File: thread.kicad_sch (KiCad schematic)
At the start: 1 part, among them U1 nRF52840

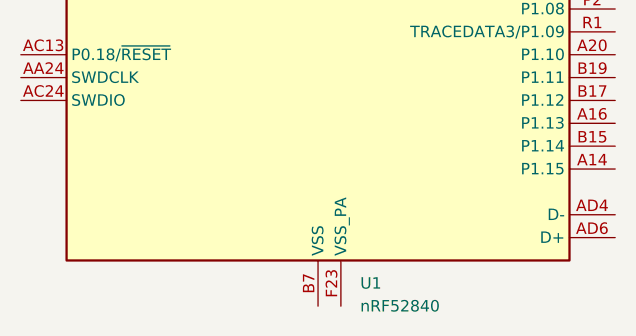
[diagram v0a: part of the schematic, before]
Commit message: Fixed schematic symbol errors
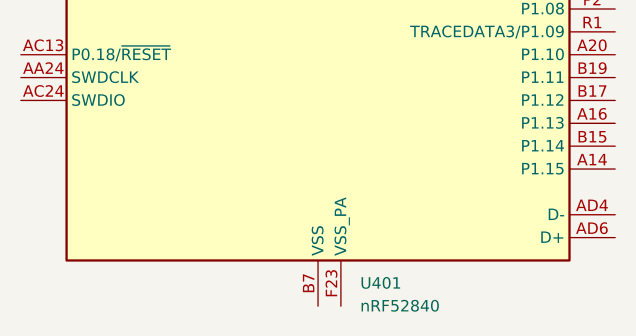
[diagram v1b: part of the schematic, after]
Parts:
- renumbered U1 to U401
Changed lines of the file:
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@@
 		(dnp no)
 		(fields_autoplaced yes)
-		(property "Reference" "U1"
+		(property "Reference" "U401"
 			(at 146.9233 212.09 0)
 			(effects
@@
 			(project ""
 				(path "/b43b7bca-e50d-42ec-8ff0-e0016dfefe0a/ab846a80-6f2e-4d25-9090-1f6af1d6fbdd"
-					(reference "U1")
+					(reference "U401")
 					(unit 1)
 				)

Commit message: Added some net labels and schematic routing
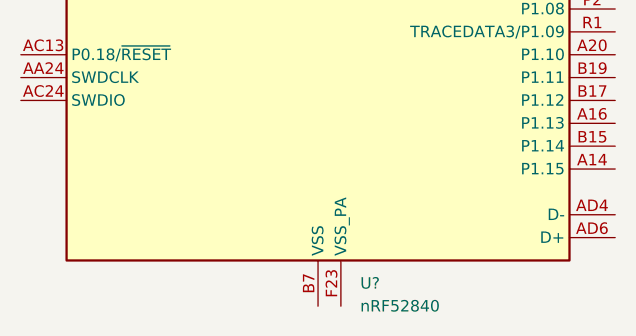
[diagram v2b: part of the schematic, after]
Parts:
- renumbered U401 to U?
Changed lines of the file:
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@@
 		(dnp no)
 		(fields_autoplaced yes)
-		(property "Reference" "U401"
+		(property "Reference" "U?"
 			(at 146.9233 212.09 0)
 			(effects
@@
 			(project ""
 				(path "/b43b7bca-e50d-42ec-8ff0-e0016dfefe0a/ab846a80-6f2e-4d25-9090-1f6af1d6fbdd"
-					(reference "U401")
+					(reference "U?")
 					(unit 1)
 				)

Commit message: Worked on schematic for DDR4 memory
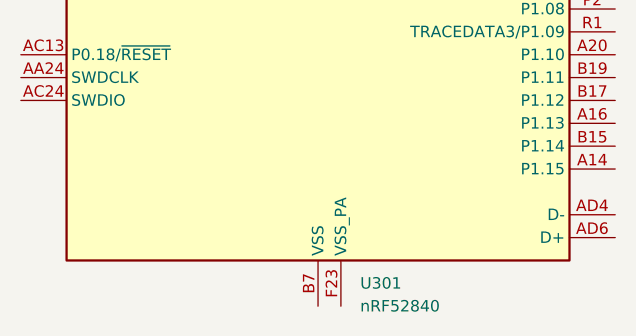
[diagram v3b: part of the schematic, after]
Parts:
- gave numbers to parts that had none: 1
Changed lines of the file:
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@@
 		(dnp no)
 		(fields_autoplaced yes)
-		(property "Reference" "U?"
+		(property "Reference" "U301"
 			(at 146.9233 212.09 0)
 			(effects
@@
 			(project ""
 				(path "/b43b7bca-e50d-42ec-8ff0-e0016dfefe0a/ab846a80-6f2e-4d25-9090-1f6af1d6fbdd"
-					(reference "U?")
+					(reference "U301")
 					(unit 1)
 				)

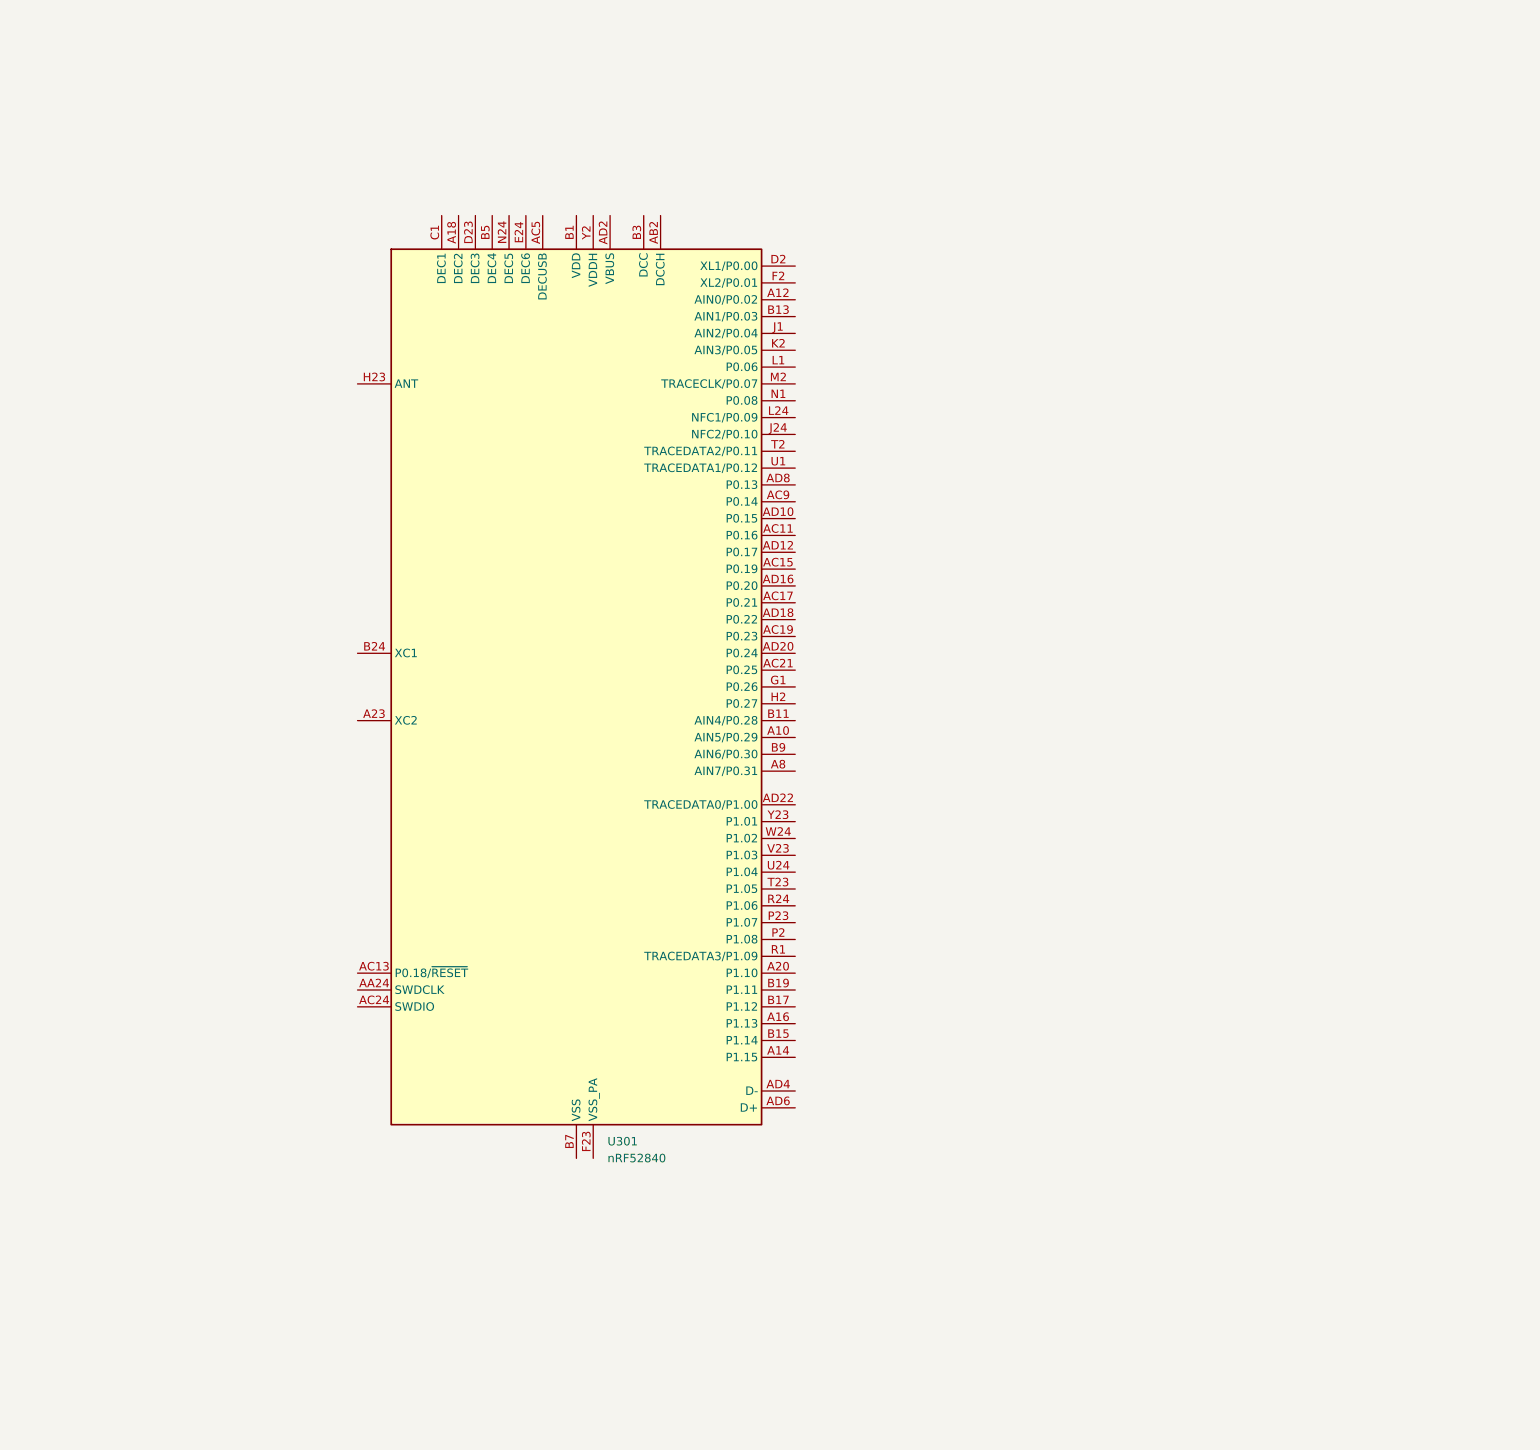
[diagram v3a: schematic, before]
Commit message: Added thread symbol and circuitry
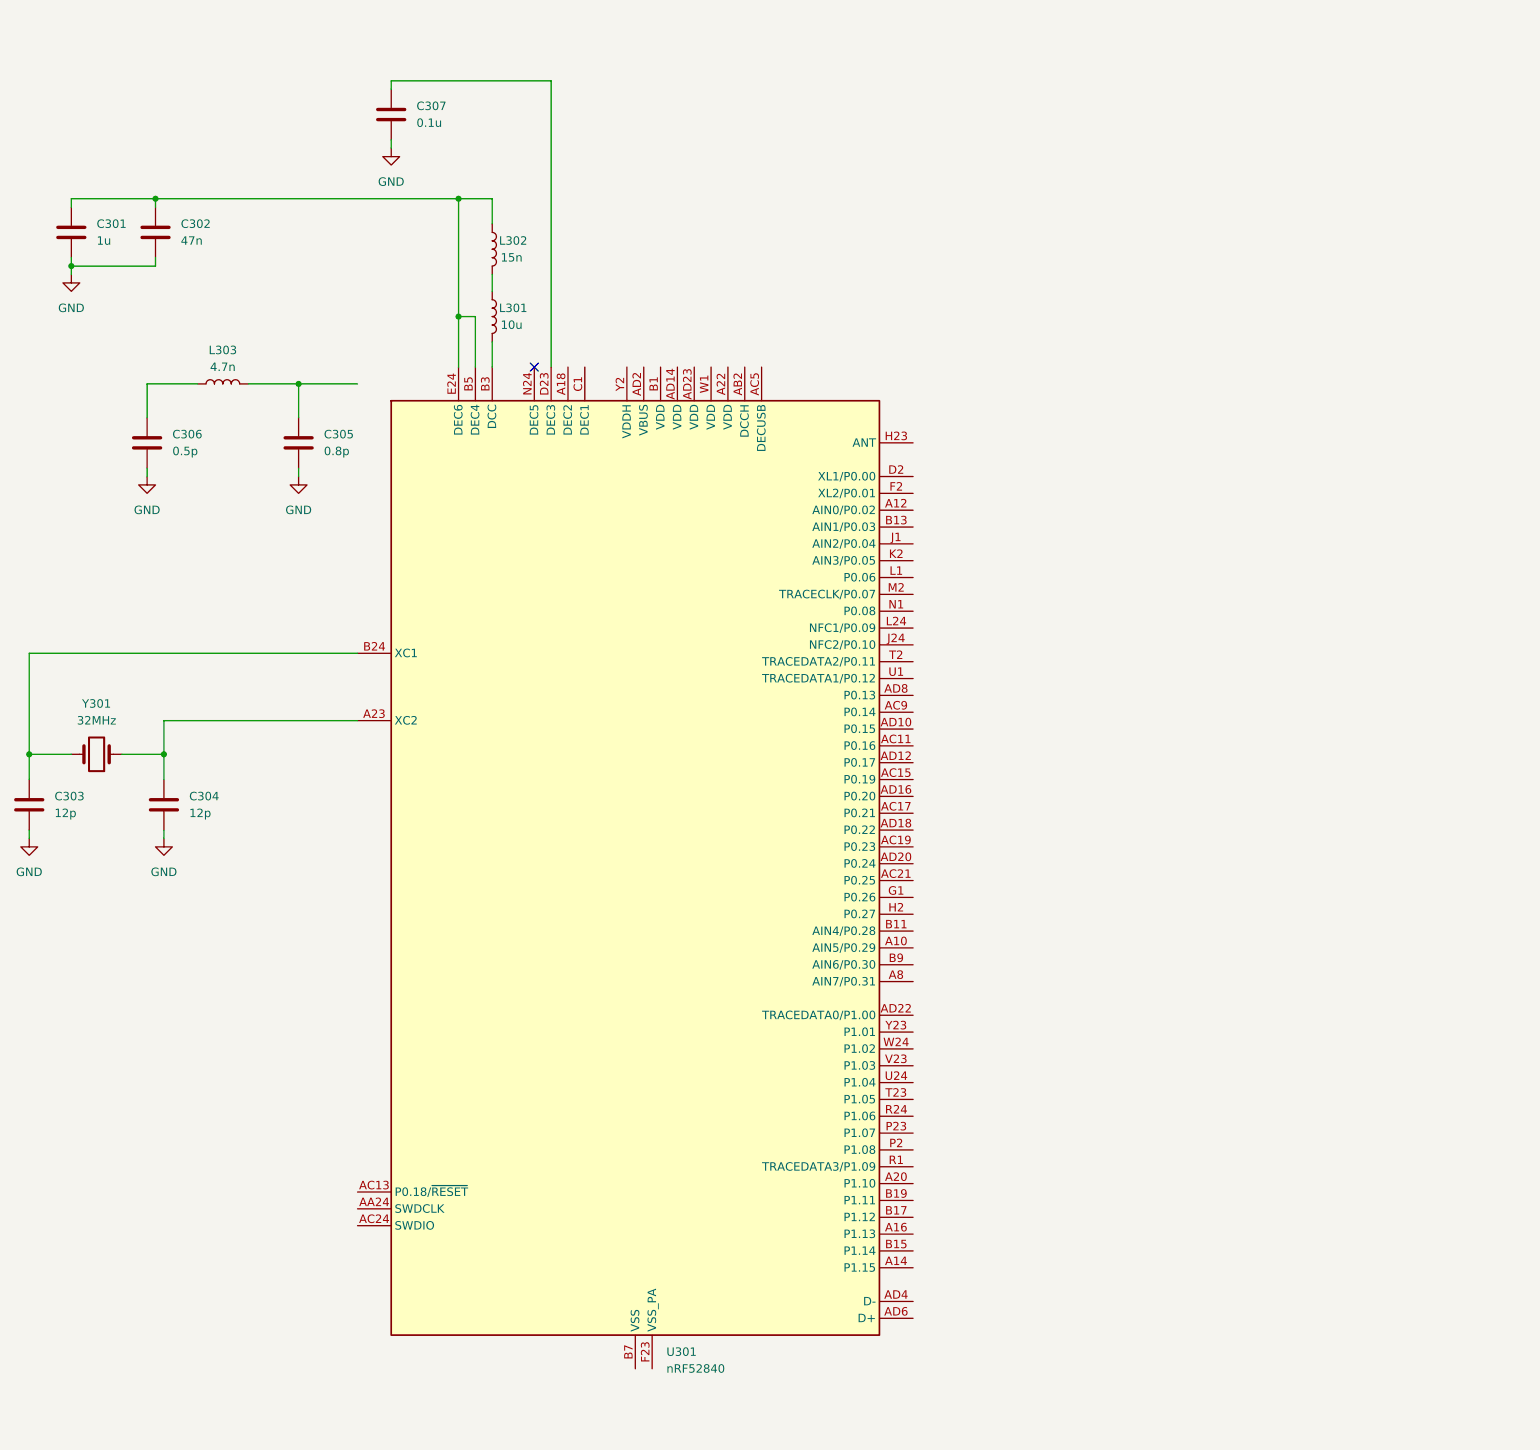
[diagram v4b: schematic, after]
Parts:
- removed U301: nRF52840, Package_DFN_QFN:Nordic_AQFN-73-1EP_7x7mm_P0.5mm, symbol MCU_Nordic:nRF52840
- added C301: 1u, symbol Device:C
- added C302: 47n, symbol Device:C
- added C303, C304: 12p, symbol Device:C
- added C305: 0.8p, symbol Device:C
- added C306: 0.5p, symbol Device:C
- added C307: 0.1u, symbol Device:C
- added L301: 10u, symbol Device:L
- added L302: 15n, symbol Device:L
- added L303: 4.7n, symbol Device:L
- added U301: nRF52840, Package_DFN_QFN:Nordic_AQFN-73-1EP_7x7mm_P0.5mm, symbol SoftServicesSymbolLibrary:nRF52840
- added Y301: 32MHz, symbol Device:Crystal
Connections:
- new net: C306.1, L303.1
- new net: C305.1, L303.2
- new net: C301.1, C302.1, L302.1, U301.B5 (DEC4), U301.E24 (DEC6)
- new net: L301.1, L302.2
- new net: L301.2, U301.B3 (DCC)
- new net: C307.1, U301.D23 (DEC3)
- new net: C304.1, U301.A23 (XC2), Y301.1
- new net: C303.1, U301.B24 (XC1), Y301.2
- new net: U301.B7 (VSS), U301.EP (VSS)
- new net GND: C301.2, C302.2, C303.2, C304.2, C305.2, C306.2, C307.2
- no-connect marks 0 -> 1

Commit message: Added power management for nRF52840
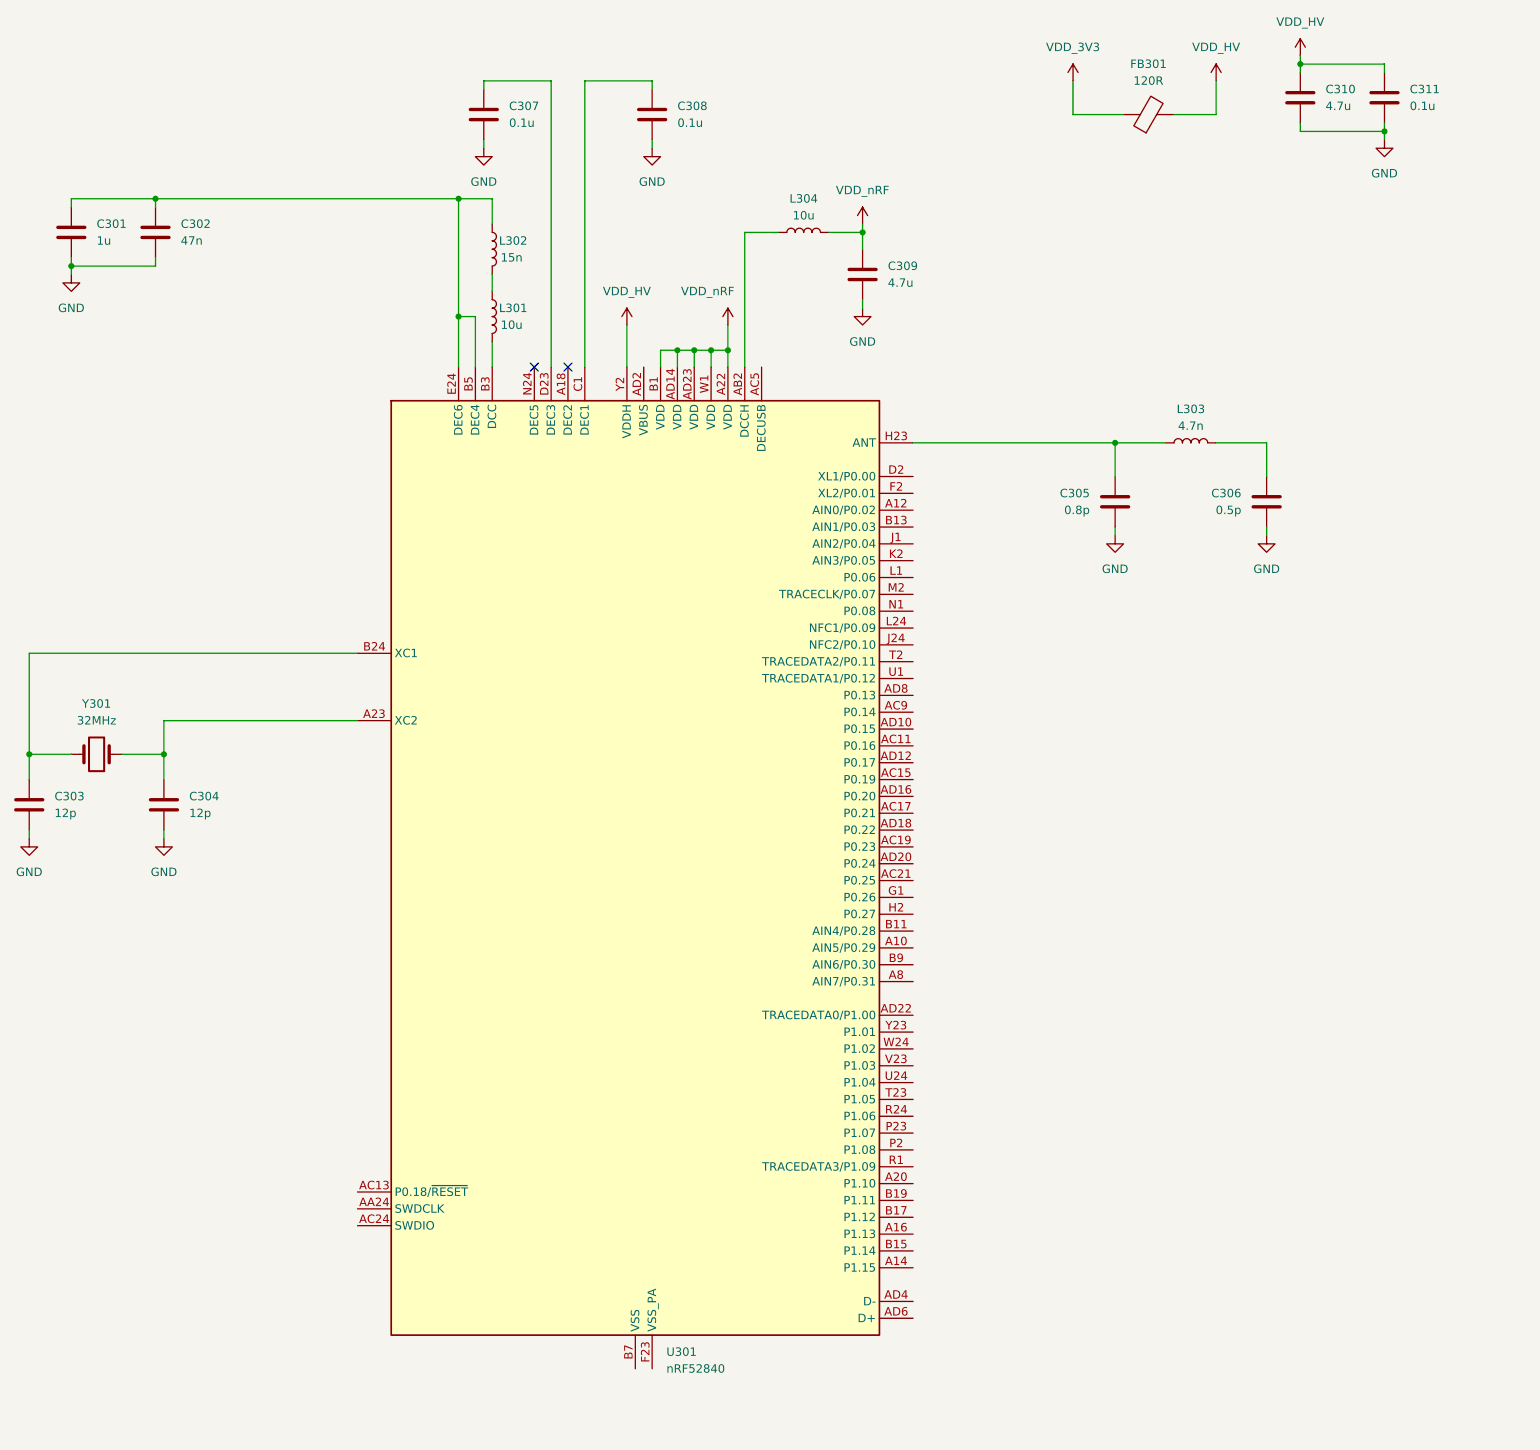
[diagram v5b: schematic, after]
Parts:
- added C308, C311: 0.1u, symbol Device:C
- added C309, C310: 4.7u, symbol Device:C
- added FB301: 120R, symbol Device:FerriteBead
- added L304: 10u, symbol Device:L
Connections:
- net GND: now also C308.2, C309.2, C310.2, C311.2
- net at C305.1, L303.2: now also U301.H23 (ANT)
- net VDD_nRF: now reaches U301.A22 (VDD)
- net VDD_nRF: now also U301.AD14 (VDD), U301.AD23 (VDD), U301.B1 (VDD), U301.W1 (VDD), C309.1, L304.2
- net at U301.AB2 (DCCH): now also L304.1
- net at U301.C1 (DEC1): now also C308.1
- net VDD_HV: now reaches U301.Y2 (VDDH)
- net VDD_HV: now also C310.1, C311.1, FB301.2
- new net VDD_3V3: FB301.1
- no-connect marks 1 -> 2
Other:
- moved on the sheet: C305, C306, C307, L303
